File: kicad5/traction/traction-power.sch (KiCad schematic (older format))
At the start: 306 parts

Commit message: Rev A.8: review round 8 response (R7-01..07, A7-N01..05) + cross-check
Review round 8 on 2ac42ed, every finding verified and classified in
docs/review-A8-disposition.md (+ .csv); findings log F90-F105.

Hardware (+Rs18/unit: SiC Rs71,040, IGBT Rs45,540):
- UASCG 74LVC1G08-Q100: ASC_CMD = ASC latch AND no driver FLT, so a
  latched DESAT drops ASC on every path, FS1B included (R7-01/A7-N01;
  NSI6611 DS Fig. 8.11 read directly)
- USCH2 74LVC3G17-Q100 buffers both latch presets and drives QDIS_CMD;
  FLT diode-OR now BAT46 for the Schmitt threshold (R7-02, R7-03, N12)
- ZSET BZT52-B5V6 to ground replaces the clamp into V5A; RENP2 removed
  (A7-N04; B5V6 keeps a 35 V load dump under the 6.5 V V_I abs max)
- RASCL = RQDL = 261 R: both TLP152 LEDs 10.3-14.8 mA, inside 10-15 mA
- dead-state pulls: RFCB on FLT_CMB_B, RASCP moved to ASC_Q
- CFLTF2 100 pF on FLT_LS_N; discharge header V15-GND-CMD-GND

Firmware contract: FW-15 always clears the ASC latch; FW-16 runs on
measured no-HV/standstill conditions (stored-pass arming otherwise),
handles the FS_GPIO1 flyback OR and injects FLT from the MCU pins;
FW-08b; FS1B_TDELAY = 0, TDUR = 100 ms; FAULT_OUT outcomes stated.

Tooling: ERC locks by net, pin number and first-match MPN per SKU
(864 checks, each new one mutation-tested); computed judges replace
fixed PASS rows; S4 static junction path + static-plate bound; VCC2
FB-sense per corner; bom-gen publishes atomically, rounds ext prices.

Gates: pins 1782/1782, ERC 864/0, design-verify 108P/14W/0F,
sim-verify 23P/6W/0F, marine 81P/19W/0F.

Co-Authored-By: Claude Opus 5.5 <noreply@anthropic.com>
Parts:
- RASCL: value 270R -> 261R; MPN R0603-270R -> R0603-261R-1%
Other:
- note added: "rev A.8 - 24 sections - 306 components"
- note removed: "rev A.7 - 24 sections - 306 components"
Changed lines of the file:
@@
 Title "Traction Inverter 220 kW — Power board (3x EconoDUAL 3 SiC)"
 Date "2026-09-23"
-Rev "A.7"
+Rev "A.8"
 Comp "Traction Inverter 220 kW pk - Power (HV), sheet 1 of 4"
 Comment1 "Inverter = Power board + Cap bank busbar + bolt-on Discharge board (all HV) + Control card (LV); safe state holds with any link lost"
@@
 DC-LINK   -   1 section
 Text Notes 32910 15450 0    60   ~ 0
-rev A.7   -   24 sections   -   306 components
+rev A.8   -   24 sections   -   306 components
 Wire Notes Line
 	32850 16400 37300 16400
@@
 P 7300 25150
 F 0 "RASCL" H 7300 24990 50  0000 C CNN
-F 1 "270R" H 7300 25320 50  0000 C CNN
+F 1 "261R" H 7300 25320 50  0000 C CNN
 F 2 "R0603" H 7300 25150 50  0001 C CNN
 F 3 "~" H 7300 25150 50  0001 C CNN
 F 4 "CLASS" H 7300 25150 50  0001 C CNN "LCSC"
-F 5 "R0603-270R" H 7300 25150 50  0001 C CNN "MPN"
+F 5 "R0603-261R-1%" H 7300 25150 50  0001 C CNN "MPN"
 	1    7300 25150
 	1    0    0    -1

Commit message: Rev A.9: review round 9 response (A8-01..03, A8-N01..N03) + cross-check
Review round 9 on 0da9014, every finding verified and classified in
docs/review-A9-disposition.md (+ .csv, 34 items); findings log F106-F119.

Hardware (+Rs29/unit: SiC Rs71,069, IGBT Rs45,569):
- PSASC/PSQD bound to the real QA01C-18 sheet (+18/-3 V; F61 had read
  the base QA01C, +20/-4 V): envelope 16.9-20.9 V, ASC entry 7.52 us,
  FW-06 end-point 906 V; discharge gate divider RQDG 1.5k (Vgs 13.4-18.1 V)
- FLT/RDY pull-ups and the diode-OR pull-up moved to V5GD (the drivers'
  VCC1; FLT/RDY abs max = VCC1), V5GD read by the MCU on PTB5
- HARNESS40 re-laid: VBAT and V5GD touch only ground in both row-by-row
  and odd/even dual-row numbering; connector family chosen at layout
- self-found: the power board's LV side ran on unswitched KL30
  (~150 mA parked) - card-side P-FET switch DMP6023LEQ on V5A with a
  slew network; resolver LDO enabled by V5A; parking drain <= 43 uA
- RFS4 = ROHM ESR03 anti-surge; CASC/CQD 50 V

Firmware contract: FW-16 energy-limited eligibility (read < 3 V or QDIS
for 2 tau); V_DC invalid while V5GD is out of window; DESATs to NVM;
BACKUP_SAFETY_PATH_FS1B = 0; motor/vehicle release rule for SPO energy.

Gates: pins 1804/1804, ERC 883/0 (new locks mutation-tested),
design-verify 116P/14W/0F, sim-verify 23P/6W/0F, marine 81P/19W/0F.

Co-Authored-By: Claude Opus 5.5 <noreply@anthropic.com>
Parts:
- CASC: MPN MLCC-100nF-25V -> MLCC-100nF-50V
- JIC: value MICROFIT3-40 -> HARNESS-2x20; symbol traction-r1:MICROFIT3-40 -> traction-r1:HARNESS-2x20-CLASS; MPN MICROFIT3-40 -> HARNESS-2x20-CLASS
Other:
- note added: "rev A.9 - 24 sections - 306 components"
- note removed: "rev A.8 - 24 sections - 306 components"
- moved on the sheet: CFHA, CFHCF, CFHCO, CFHCT, CFHFS, CFHSI, CFHSN, CFHVR, CFLA, CFLCF, CFLCO, CFLCT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

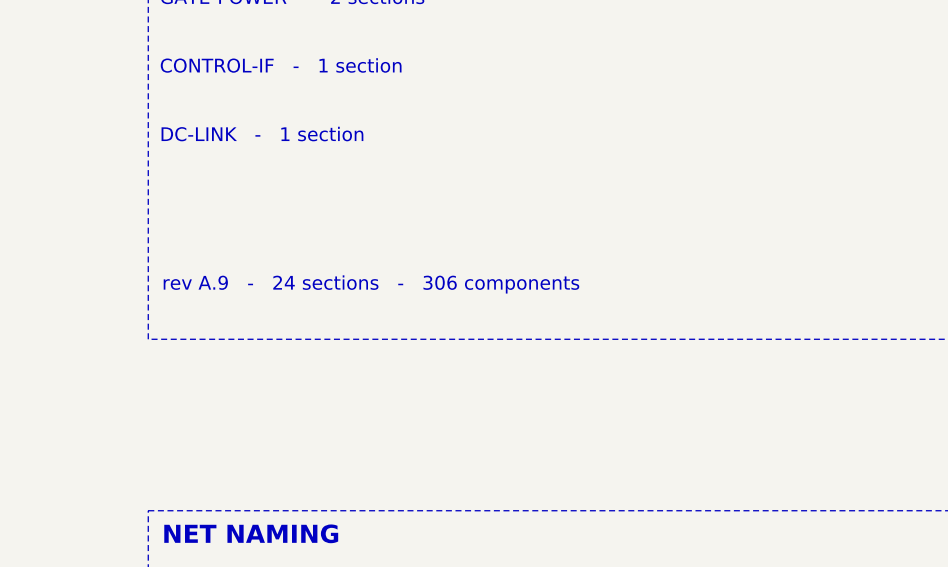
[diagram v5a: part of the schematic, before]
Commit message: Rev A.10: schematic rechecks of A.9 (A9-S01, S9-01, S9-02)
Two schematic-only rechecks of 7235337 kept every A.9 correction;
dispositioned in docs/review-A10-disposition.md (+ .csv); F120-F122.

- RDY_HS/RDY_LS now reach UAND1/UAND2 through a third 74LVC3G17-Q100
  (USCH3, RRDB dead-state pull-down): the open-drain lines rose at
  ~20-100 ns/V against the 74LVC1G11's 10 ns/V limit (A9-S01; reverses
  the round-7/8 "state-benign" rejection)
- RASCG = ROHM ESR03EZPF2201 (0.27 W at 85 C): it carries up to 0.12 W
  for as long as ASC is held; 2.2 k kept for the ASC timing (S9-01)
- discharge sheet note 66k bleeder; gate divider stated as 13.3-18.2 V
  (a divider, not a clamp); A9 disposition quotes the final harness map

+Rs11/unit (SiC Rs71,080, IGBT Rs45,580).
Gates: pins 1815/1815, ERC 891/0 (new locks mutation-tested),
design-verify 118P/14W/0F, sim-verify 23P/6W/0F, marine 81P/19W/0F.

Co-Authored-By: Claude Opus 5.5 <noreply@anthropic.com>
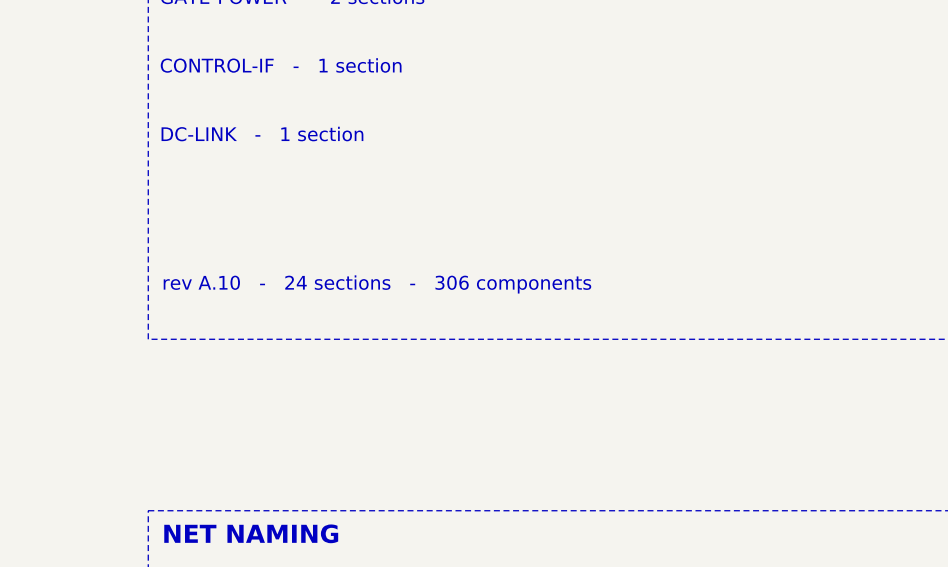
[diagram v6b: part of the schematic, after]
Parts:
- RASCG: MPN R0603-2k2 -> ESR03EZPF2201
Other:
- note added: "rev A.10 - 24 sections - 306 components"
- note removed: "rev A.9 - 24 sections - 306 components"
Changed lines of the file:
@@
 Title "Traction Inverter 220 kW — Power board (3x EconoDUAL 3 SiC)"
 Date "2026-09-23"
-Rev "A.9"
+Rev "A.10"
 Comp "Traction Inverter 220 kW pk - Power (HV), sheet 1 of 4"
 Comment1 "Inverter = Power board + Cap bank busbar + bolt-on Discharge board (all HV) + Control card (LV); safe state holds with any link lost"
@@
 DC-LINK   -   1 section
 Text Notes 32910 15450 0    60   ~ 0
-rev A.9   -   24 sections   -   306 components
+rev A.10   -   24 sections   -   306 components
 Wire Notes Line
 	32850 16400 37300 16400
@@
 F 3 "~" H 7300 25550 50  0001 C CNN
 F 4 "CLASS" H 7300 25550 50  0001 C CNN "LCSC"
-F 5 "R0603-2k2" H 7300 25550 50  0001 C CNN "MPN"
+F 5 "ESR03EZPF2201" H 7300 25550 50  0001 C CNN "MPN"
 	1    7300 25550
 	1    0    0    -1

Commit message: Rev A.11: review round 12 response (R1-F01..F28, R2-F01..F35) + datasheet archive
Two whole-system reviews of 4544715 (28 + 35 findings), dispositioned line by
line in docs/review-A11-disposition.md (+ CSV). Twelve real findings fixed
(F123-F134); the rest are tracked gates, firmware-owned, wording or out of the
schematic release's scope. No power-stage, capacitor or topology change.

Hardware / contract:
- SS6 release rule (a) is an energy inequality: winding energy 1.5*L*I^2 plus the
  back-EMF work during the decay, closed-form screen while E < V0, diode-bridge
  simulation otherwise; screening rows (WARN) per SKU
- Resolver exciter rewired as a textbook MFB (1.5 nF / 220 pF): the drawn network
  had the feedback pair swapped, |H(10 kHz)| 0.18 -> 1.85; SWG given its 47 pF load
- V_DC bias: "MGJ2D150505SC" was not an existing order code and no MGJ2 is
  reinforced above 150 Vrms -> TI UCC12050 per channel (V_IOWM 1200 Vrms /
  1697 VDC) behind its own NCV4276C from V15
- Hall: 100 k pull-downs drawn (claimed since A.4); LEM HC5FW drawn with its
  real terminals (1 V_ref, 2 V_out, 3 Gnd, 4 U_C, E1-E4)
- Resolver inputs 10 k / 10 k with rescaled, symmetric filter caps: a wire shorted
  to KL30 injected 23 mA into an SDADC pin against the 3 mA limit
- LV-entry TVS bound explicitly as TPSMC24CA-VR (24 V stand-off, AEC-Q101): the
  classic part the notes described conducts at a 24 V jump start; the OEM's
  load-dump source resistance becomes gate 23
- CSB5 1 uF 0805 (VREF5 inside the FS26 window), ALM2402 as HTSSOP14-PWP,
  on-board NTCs RTAMB/RTHS, kicad5-verify empty-set guard
- Contract wording: FW-05 in instantaneous amperes with a validity window, the
  "BMS limit 0" row split from "contactor open", NVM logging queued behind the
  safe action, FW-02 tau check demoted to plausibility (EOL measurement in dfm),
  FW-18 "unknown, never safe", S6 double-update stated; stale pin-40 / LQFP-176 /
  "inside 6 us" / ALT-field texts corrected; CAN termination DNP option

Doc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
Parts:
- added RPD3, RPD4, RPD5, RPD6, RPD7, RPD8, RPD9: 10k, R0603, symbol traction-r1:R
- C5B1: renamed from C5C1; value 1uF -> 10uF; footprint C0603 -> C1206; MPN MLCC-1uF-25V -> MLCC-10uF-16V-X7R
- C5B2: renamed from PSASC; value QA01C-18 -> 100nF; footprint SIP7 -> C0603; symbol traction-r1:QA01C-18 -> traction-r1:C; MPN QA01C-18 -> MLCC-100nF-25V
- C5C1: renamed from UASC; value TLP152 -> 10uF; footprint SO6 -> C1206; symbol traction-r1:TLP152 -> traction-r1:C; LCSC C17255258 -> CLASS; MPN TLP152 -> MLCC-10uF-16V-X7R
- C5C2: renamed from CASC; MPN MLCC-100nF-50V -> MLCC-100nF-25V
- C5G1: renamed from CB15I; value 10uF -> 1uF; footprint C1210 -> C0805; MPN MLCC-10uF-50V -> MLCC-1uF-50V
- C5G2: renamed from CB15O1; value 22uF -> 10uF; footprint C1210 -> C1206; MPN MLCC-22uF-50V -> MLCC-10uF-25V
- C5LB1: renamed from CASCD; value 12nF -> 1uF; footprint C0603 -> C0805; MPN MLCC-12nF-50V-C0G -> MLCC-1uF-50V
- C5LB2: renamed from DASCR; value 1N4148WS -> 10uF; footprint SOD323 -> C1206; symbol traction-r1:D -> traction-r1:C; LCSC C2128 -> CLASS; MPN 1N4148WS -> MLCC-10uF-16V-X7R
- C5LC1: renamed from RASCG; value 2.2k -> 1uF; footprint R0603 -> C0805; symbol traction-r1:R -> traction-r1:C; MPN ESR03EZPF2201 -> MLCC-1uF-50V
- C5LC2: renamed from RASCL; value 261R -> 10uF; footprint R0603 -> C1206; symbol traction-r1:R -> traction-r1:C; MPN R0603-261R-1% -> MLCC-10uF-16V-X7R
- CASC: renamed from CLVH1; value 4.7uF -> 100nF; footprint C1206 -> C0603; MPN MLCC-4.7uF-50V -> MLCC-100nF-50V
- CASCD: renamed from CLVH2; value 4.7uF -> 12nF; footprint C1206 -> C0603; MPN MLCC-4.7uF-50V -> MLCC-12nF-50V-C0G
- CB15C: renamed from CLDC; value 220pF -> 470pF
- CB15CC: renamed from DB15; value SS34 -> 100nF; footprint SMA -> C0603; symbol traction-r1:D -> traction-r1:C; MPN SS34 -> MLCC-CLASS
- CB15I: renamed from LB15; value XAL4040-103MEC -> 10uF; footprint XAL4040 -> C1210; symbol traction-r1:L -> traction-r1:C; MPN XAL4040-103MEC -> MLCC-10uF-50V
- CB15O1: renamed from RB15C; value 2k -> 22uF; footprint R0603 -> C1210; symbol traction-r1:R -> traction-r1:C; MPN R0603-CLASS -> MLCC-22uF-50V
- CB15O2: renamed from RB15F1; value 110k -> 22uF; footprint R0603 -> C1210; symbol traction-r1:R -> traction-r1:C; MPN R0603-1% -> MLCC-22uF-50V
- CB15S: renamed from RB15F2; value 9.53k -> 47nF; footprint R0603 -> C0603; symbol traction-r1:R -> traction-r1:C; MPN R0603-1% -> MLCC-CLASS
- CLD15: renamed from RB15Q; value 80.6k -> 22uF; footprint R0603 -> C0603; symbol traction-r1:R -> traction-r1:C; MPN R0603-CLASS -> MLCC-CLASS
- CLDC: renamed from RLD1; value 49.9k -> 220pF; footprint R0603 -> C0603; symbol traction-r1:R -> traction-r1:C; MPN R0603-CLASS -> MLCC-CLASS
- CLVH2: renamed from DRL; value NRVBAF360T3G -> 4.7uF; footprint SMA-flat -> C1206; symbol traction-r1:D -> traction-r1:C; MPN NRVBAF360T3G -> MLCC-4.7uF-50V
- CLVL1: renamed from C5G1; value 1uF -> 4.7uF; footprint C0805 -> C1206; MPN MLCC-1uF-50V -> MLCC-4.7uF-50V
- CLVL2: renamed from C5G2; value 10uF -> 4.7uF; MPN MLCC-10uF-25V -> MLCC-4.7uF-50V
- DASCR: renamed from DRH; value NRVBAF360T3G -> 1N4148WS; footprint SMA-flat -> SOD323; LCSC CLASS -> C2128; MPN NRVBAF360T3G -> 1N4148WS
- DB15: renamed from RLD2; value 10k -> SS34; footprint R0603 -> SMA; symbol traction-r1:R -> traction-r1:D; MPN R0603-CLASS -> SS34
- DRH: renamed from DTVL; value TPSMC24CA -> NRVBAF360T3G; footprint SMC -> SMA-flat; LCSC C1975284 -> CLASS; MPN TPSMC24CA -> NRVBAF360T3G
- DRL: renamed from RGDLE; value 100k -> NRVBAF360T3G; footprint R0603 -> SMA-flat; symbol traction-r1:R -> traction-r1:D; MPN R0603-CLASS -> NRVBAF360T3G
- DTVH: renamed from FL1; value MF-LSMF300/24X-2 -> TPSMC24CA-VR; footprint PTC2920 -> SMC; symbol traction-r1:F -> traction-r1:D; LCSC C719172 -> C1975284; MPN MF-LSMF300/24X-2 -> TPSMC24CA-VR
- DTVL: renamed from UB15; value TPS55340QRTERQ1 -> TPSMC24CA-VR; footprint WQFN16 -> SMC; symbol traction-r1:TPS55340QRTERQ1 -> traction-r1:D; LCSC C2070860 -> C1975284; MPN TPS55340QRTERQ1 -> TPSMC24CA-VR
- FH1: renamed from LFL1; value FB-120R-3A -> MF-LSMF300/24X-2; footprint FB1206 -> PTC2920; symbol traction-r1:L -> traction-r1:F; LCSC CLASS -> C719172; MPN FB-120R-3A -> MF-LSMF300/24X-2
- FL1: renamed from ULDO15; value NCV4276CDTADJRKG -> MF-LSMF300/24X-2; footprint DPAK5 -> PTC2920; symbol traction-r1:NCV4276CDTADJRKG -> traction-r1:F; LCSC CLASS -> C719172; MPN NCV4276CDTADJRKG -> MF-LSMF300/24X-2
- JIC: renamed from RPD4; value 10k -> HARNESS-2x20; footprint R0603 -> MicroFit40; symbol traction-r1:R -> traction-r1:HARNESS-2x20-CLASS; MPN R0603-10k -> HARNESS-2x20-CLASS
- LB15: renamed from JIC; value HARNESS-2x20 -> XAL4040-103MEC; footprint MicroFit40 -> XAL4040; symbol traction-r1:HARNESS-2x20-CLASS -> traction-r1:L; MPN HARNESS-2x20-CLASS -> XAL4040-103MEC
- LFH1: renamed from UGDL; value NCV4276CDT50RKG -> FB-120R-3A; footprint DPAK -> FB1206; symbol traction-r1:NCV4276CDT50RKG -> traction-r1:L; MPN NCV4276CDT50RKG -> FB-120R-3A
- LFL1: renamed from CB15C; value 470pF -> FB-120R-3A; footprint C0603 -> FB1206; symbol traction-r1:C -> traction-r1:L; MPN MLCC-CLASS -> FB-120R-3A
- PS5B, PS5C: value MGJ2D150505SC -> UCC12050DVER; footprint SIP7 -> SOIC16W; symbol traction-r1:MGJ2D150505SC -> traction-r1:UCC12050DVER; MPN MGJ2D150505SC -> UCC12050DVER
- PSASC: renamed from RASCPD; value 10k -> QA01C-18; footprint R0603 -> SIP7; symbol traction-r1:R -> traction-r1:QA01C-18; MPN R0603-10k -> QA01C-18
- RASCG: renamed from DTVH; value TPSMC24CA -> 2.2k; footprint SMC -> R0603; symbol traction-r1:D -> traction-r1:R; LCSC C1975284 -> CLASS; MPN TPSMC24CA -> ESR03EZPF2201
- RASCL: renamed from FH1; value MF-LSMF300/24X-2 -> 261R; footprint PTC2920 -> R0603; symbol traction-r1:F -> traction-r1:R; LCSC C719172 -> CLASS; MPN MF-LSMF300/24X-2 -> R0603-261R-1%
- RASCPD: renamed from LFH1; value FB-120R-3A -> 10k; footprint FB1206 -> R0603; symbol traction-r1:L -> traction-r1:R; MPN FB-120R-3A -> R0603-10k
- RB15C: renamed from RHWID; value 10k -> 2k; MPN R0603-10k-1% -> R0603-CLASS
- RB15F1: renamed from RPD0; value 10k -> 110k; MPN R0603-10k -> R0603-1%
- RB15F2: renamed from RPD1; value 10k -> 9.53k; MPN R0603-10k -> R0603-1%
- RB15Q: renamed from RPD10; value 10k -> 80.6k; MPN R0603-10k -> R0603-CLASS
- RGDLE: renamed from CB15O2; value 22uF -> 100k; footprint C1210 -> R0603; symbol traction-r1:C -> traction-r1:R; MPN MLCC-22uF-50V -> R0603-CLASS
- RHWID: renamed from RPD5; MPN R0603-10k -> R0603-10k-1%
- RLD1: renamed from RPD2; value 10k -> 49.9k; MPN R0603-10k -> R0603-CLASS
- RLD2: renamed from RPD3; MPN R0603-10k -> R0603-CLASS
- U5LB: renamed from C5B1; value 1uF -> NCV4276CDT50RKG; footprint C0603 -> DPAK; symbol traction-r1:C -> traction-r1:NCV4276CDT50RKG; MPN MLCC-1uF-25V -> NCV4276CDT50RKG
- U5LC: renamed from C5B2; value 100nF -> NCV4276CDT50RKG; footprint C0603 -> DPAK; symbol traction-r1:C -> traction-r1:NCV4276CDT50RKG; MPN MLCC-100nF-25V -> NCV4276CDT50RKG
- UASC: renamed from ZASC; value BZT52-C5V1 -> TLP152; footprint SOD123 -> SO6; symbol traction-r1:D -> traction-r1:TLP152; LCSC CLASS -> C17255258; MPN BZT52-C5V1 -> TLP152
- UB15: renamed from CB15S; value 47nF -> TPS55340QRTERQ1; footprint C0603 -> WQFN16; symbol traction-r1:C -> traction-r1:TPS55340QRTERQ1; LCSC CLASS -> C2070860; MPN MLCC-CLASS -> TPS55340QRTERQ1
- UGDL: renamed from CB15CC; value 100nF -> NCV4276CDT50RKG; footprint C0603 -> DPAK; symbol traction-r1:C -> traction-r1:NCV4276CDT50RKG; MPN MLCC-CLASS -> NCV4276CDT50RKG
- ULDO15: renamed from CLD15; value 22uF -> NCV4276CDTADJRKG; footprint C0603 -> DPAK5; symbol traction-r1:C -> traction-r1:NCV4276CDTADJRKG; MPN MLCC-CLASS -> NCV4276CDTADJRKG
- ZASC: renamed from CLVL1; value 4.7uF -> BZT52-C5V1; footprint C1206 -> SOD123; symbol traction-r1:C -> traction-r1:D; MPN MLCC-4.7uF-50V -> BZT52-C5V1
- renumbered CLVL2 to CLVH1, RPD6 to RPD0, RPD7 to RPD1, RPD8 to RPD10, RPD9 to RPD2
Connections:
- net labels added: V5SB, V5SC
- wire segments 835 -> 875
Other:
- note added: "rev A.11 - 24 sections - 313 components"
- note removed: "rev A.10 - 24 sections - 306 components"
- moved on the sheet: C5B1, C5C2, C5G1, C5G2, C5LB1, CASC, CASCD, CB15C, CB15I, CFHA, CFHCF, CFHCO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
